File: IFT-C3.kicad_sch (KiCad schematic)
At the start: 45 parts, among them IC1 DIO5508XS8, J1 Conn_01x04_Socket, J2 Conn_01x10_Pin, J3 USB4085-GF-A_REVB, J4 Conn_01x10_Pin, J5 SJ-3523-SMT-TR, J7 Conn_01x02, Q12 Q_Photo_NPN, Q2 Q_NMOS_GSD, SW1 SW_Push_Dual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

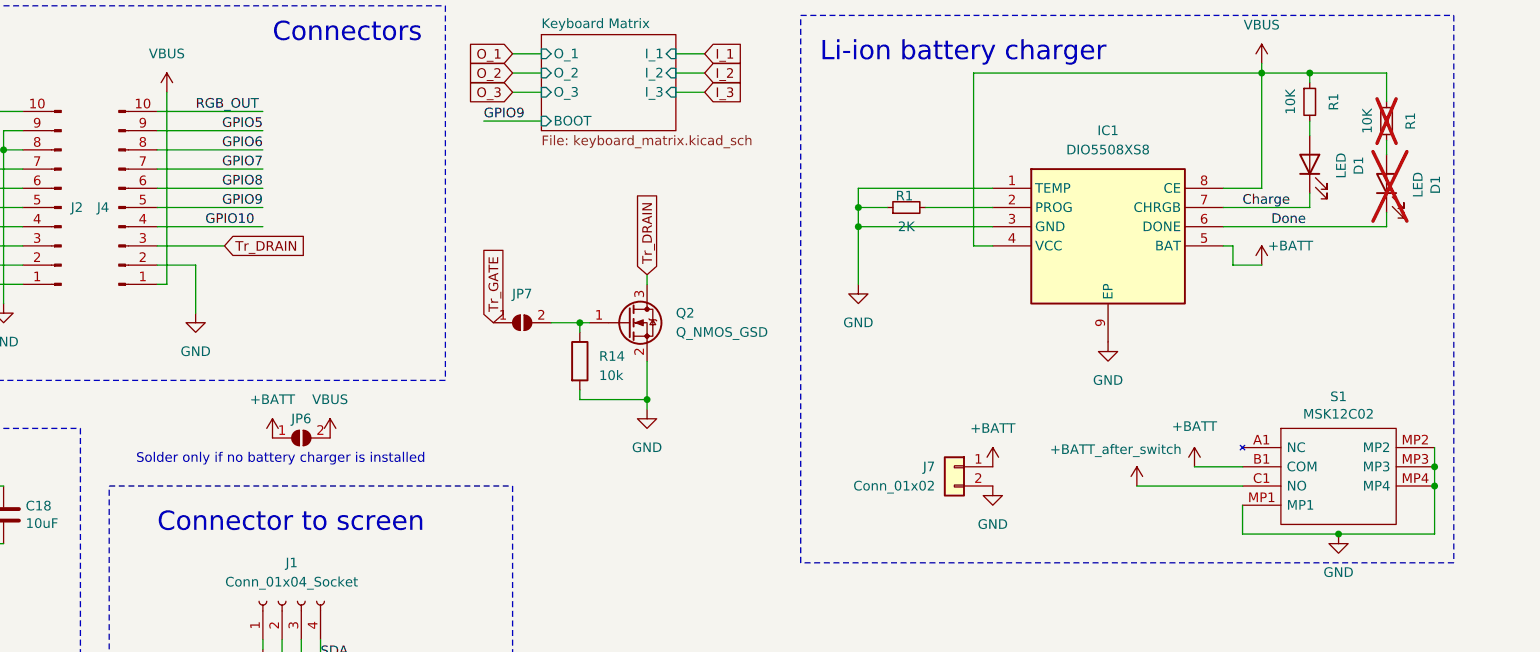
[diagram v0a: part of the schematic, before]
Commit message: RGB LEDs moved, almost ready for prob
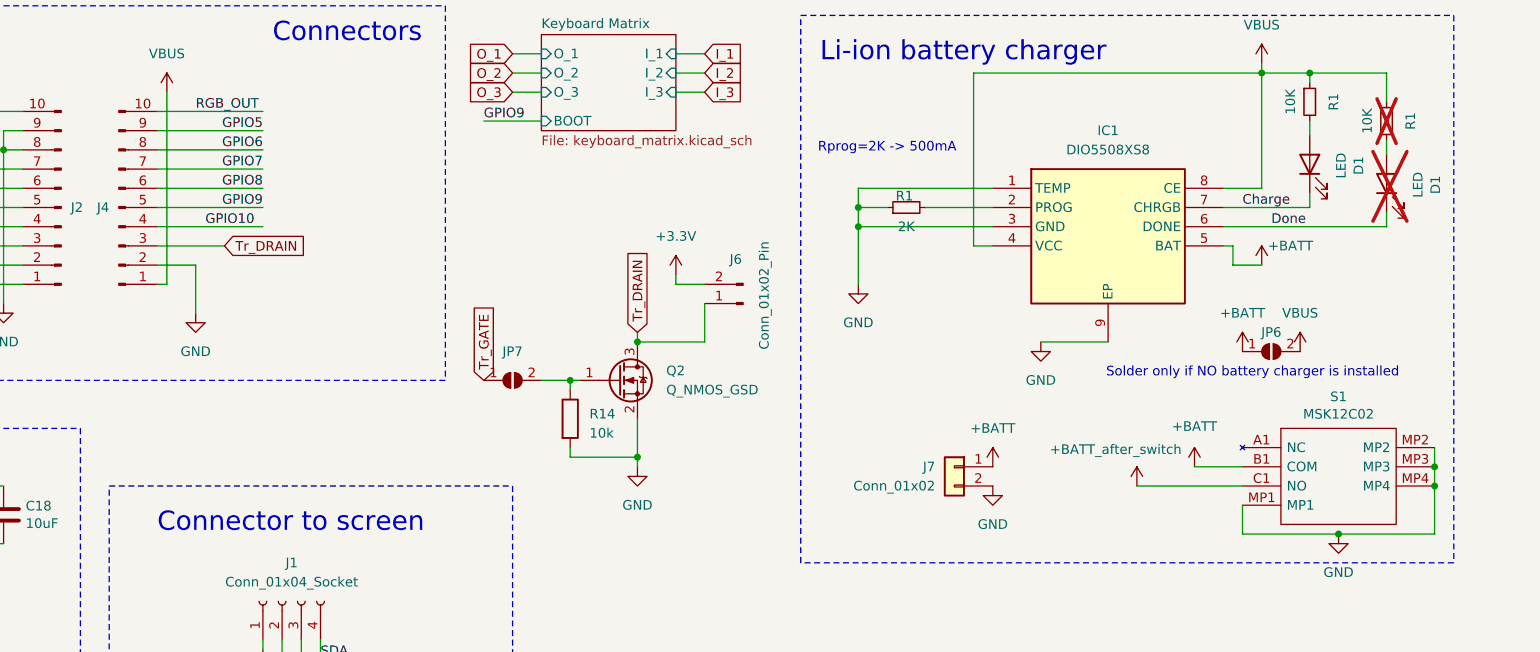
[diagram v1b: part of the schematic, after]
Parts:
- added J6: Conn_01x02_Pin, Motors:Vybronics_VZ30C1T8219732L, symbol Connector:Conn_01x02_Pin
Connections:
- net +3.3V: now also J6.2 (Pin_2)
- net Tr_DRAIN: now also J6.1 (Pin_1)
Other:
- note added: "Rprog=2K -> 500mA"
- note added: "Solder only if NO battery charger is installed"
- note removed: "Solder only if no battery charger is installed"
- moved on the sheet: JP6, JP7, Q2, R14

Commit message: Uniformed values for R and C for a better BOM
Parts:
- C18: value 10uF -> 10u
- C5: value 100nF -> 100n
- R14: value 10k -> 10K
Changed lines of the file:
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@@
 			)
 		)
-		(property "Value" "100nF"
+		(property "Value" "100n"
 			(at 91.44 62.23 0)
 			(effects
@@
 			)
 		)
-		(property "Value" "10uF"
+		(property "Value" "10u"
 			(at 93.091 158.623 0)
 			(effects
@@
 			)
 		)
-		(property "Value" "10k"
+		(property "Value" "10K"
 			(at 167.64 146.685 0)
 			(effects
@@
 			)
 		)
-		(property "Value" "10uF"
+		(property "Value" "10u"
 			(at 82.931 158.623 0)
 			(effects

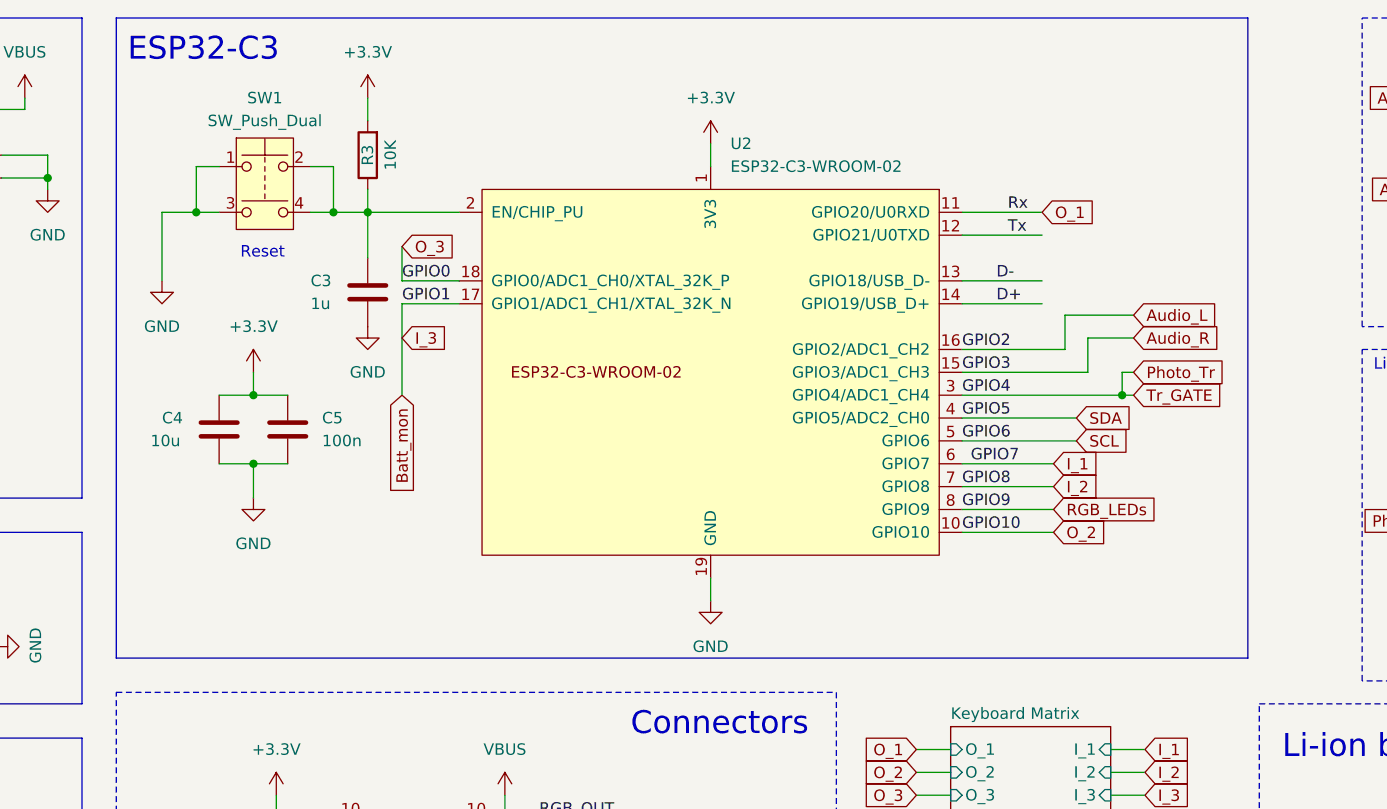
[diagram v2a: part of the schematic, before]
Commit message: Bugs fixed (buttons and OLED holes)
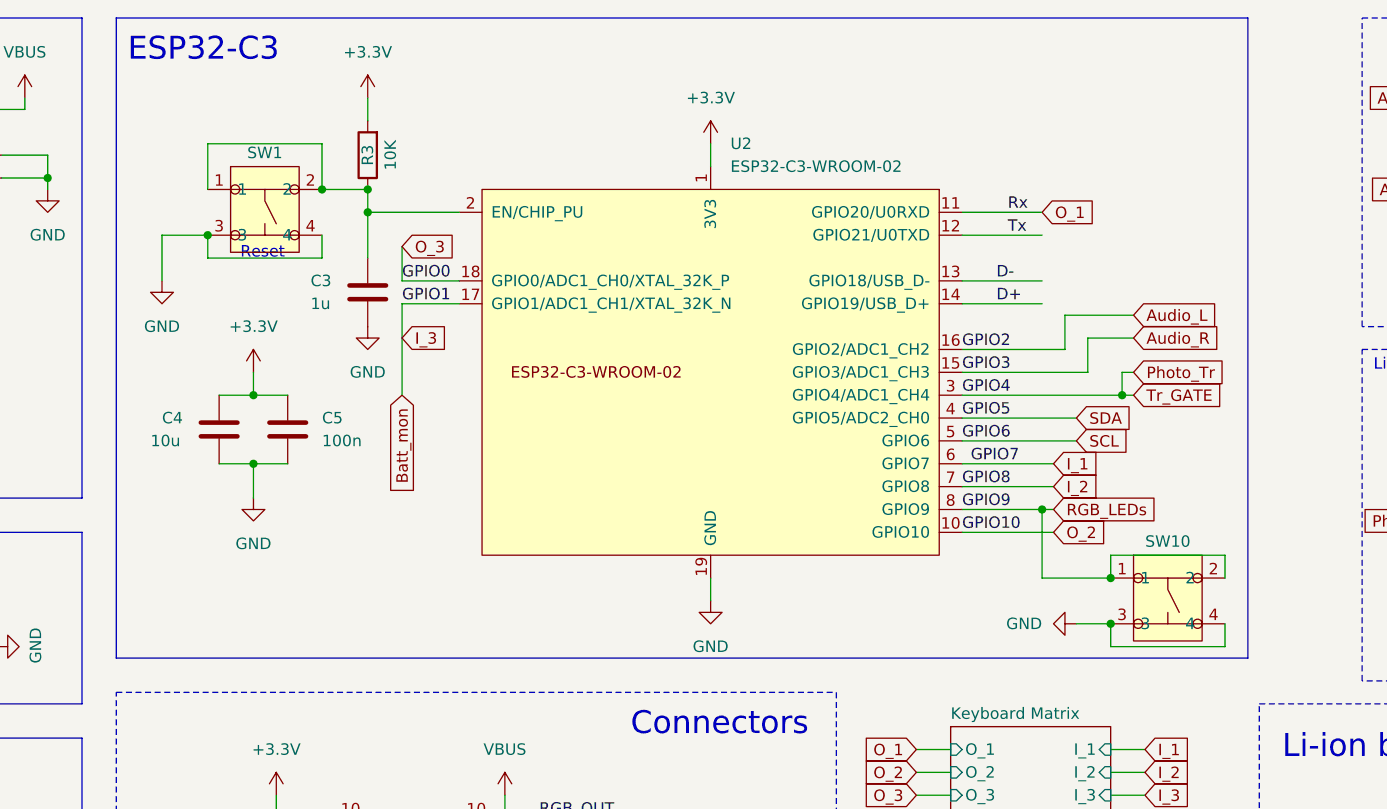
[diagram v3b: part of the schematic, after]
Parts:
- removed SW1: SW_Push_Dual, footprints:PTS526SM15SMTR2LFS, symbol Switch:SW_Push_Dual
- added SW1, SW10: PTS526_SK15_SMTR2_LFS, footprints:PTS526SK15SMTR2LFS, symbol PTS526_SK15_SMTR2_LFS:PTS526_SK15_SMTR2_LFS
- S1: footprint Local footprints:MSK12C02 -> footprints:MSK12C02
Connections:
- net GND: now also SW1.3, SW1.4, SW10.3, SW10.4
- net RGB_LEDs: now also SW10.1, SW10.2
- net at C3.1, R3.1, U2.2 (EN/CHIP_PU): now also SW1.1, SW1.2
